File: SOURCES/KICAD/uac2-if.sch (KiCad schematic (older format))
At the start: 55 parts, among them IC24 XE216-512-TQ128, IC25 NCP4681DSQ25T1G, IC26 IS25LQ080B, IC301 NC7WZ07, X5 CONN_01X04, X6 USB_B, X7 CONN_02X10

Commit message: New PCB layout
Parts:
- removed C241: 10n0, rklib:C0805-X7R, symbol C
- removed C242, C243, C245, C301: 100n, rklib:C0805-X7R, symbol C
- removed C244: 1n00, rklib:C0805-X7R, symbol C
- removed C246, C247: 10u0, rklib:C0805-X7R, symbol C
- removed R249, R301, R302: 10K0, rklib:C0805-RES, symbol R
- removed R252: 33R0, Resistors_SMD:R_Array_Convex_4x0603, symbol R_PACK4
- removed R259: 100K, rklib:C0805-RES, symbol R
- removed X6: USB_B, Connect:USB_B, symbol USB_B
- removed X7: CONN_02X10, Pin_Headers:Pin_Header_Straight_2x10, symbol CONN_02X10
- added C201: CAP_10n0_50V_X7R_0805, rklib:C0805-X7R, symbol CAP_10n0_50V_X7R_0805
- added C202, C203, C204, C207: CAP_100n_50V_X7R_0805, rklib:C0805-X7R, symbol CAP_100n_50V_X7R_0805
- added C205, C206: CAP_10u0_25V_X5R_0805, rklib:C0805-X7R, symbol CAP_10u0_25V_X5R_0805
- added C208: CAP_1n00_50V_X7R_0805, rklib:C0805-X7R, symbol CAP_1n00_50V_X7R_0805
- added R201, R204, R205: RES_10K0_1%_0.125W_Thick_0805, rklib:C0805-RES, symbol RES_10K0_1%_0.25W_Thin_0805
- added R206: 51R0, Resistors_SMD:R_Array_Convex_4x0603, symbol R_Pack04
- added R213, R214: RES_2K00_1%_0.125W_Thick_0805, rklib:C0805-RES, symbol RES_4K70_1%_0.125W_Thick_0805
- added R215: RES_100K_1%_0.125W_Thick_0805, rklib:C0805-RES, symbol RES_100K_1%_0.125W_Thick_0805
- added X201: USB_B, Connect:USB_B, symbol USB_B
- added X203: HDR_02x10, Pin_Headers:Pin_Header_Straight_2x10, symbol Conn_02x10_Odd_Even
- IC204: renamed from IC26; value IS25LQ080B -> IS25LP080D
- R202: renamed from R250; value 33R0 -> 51R0
- R207: renamed from R253; value 33R0 -> 51R0
- R208: renamed from R254; value 33R0 -> 51R0
- R211: renamed from R257; value 33R0 -> 51R0
- R212: renamed from R258; value 33R0 -> 51R0
- X202: renamed from X5; symbol CONN_01X04 -> Conn_01x04
- renumbered C248 to C209, C249 to C210, C250 to C211, C251 to C212, C252 to C213, C253 to C214, C254 to C215, C255 to C216, C256 to C217, C257 to C218, C258 to C219, C259 to C220, C260 to C221, C261 to C222, C262 to C223, C263 to C224, C264 to C225, C265 to C226, C266 to C227, C267 to C228, C268 to C229, C269 to C230, C270 to C231, C271 to C232, C272 to C233, D65 to D201, IC301 to IC201, IC24 to IC202, IC25 to IC203, OSC1 to OSC201, R251 to R203, R255 to R209, R256 to R210
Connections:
- net labels removed: xSCL, xSDA
- wire segments 173 -> 181
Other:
- moved on the sheet: D201

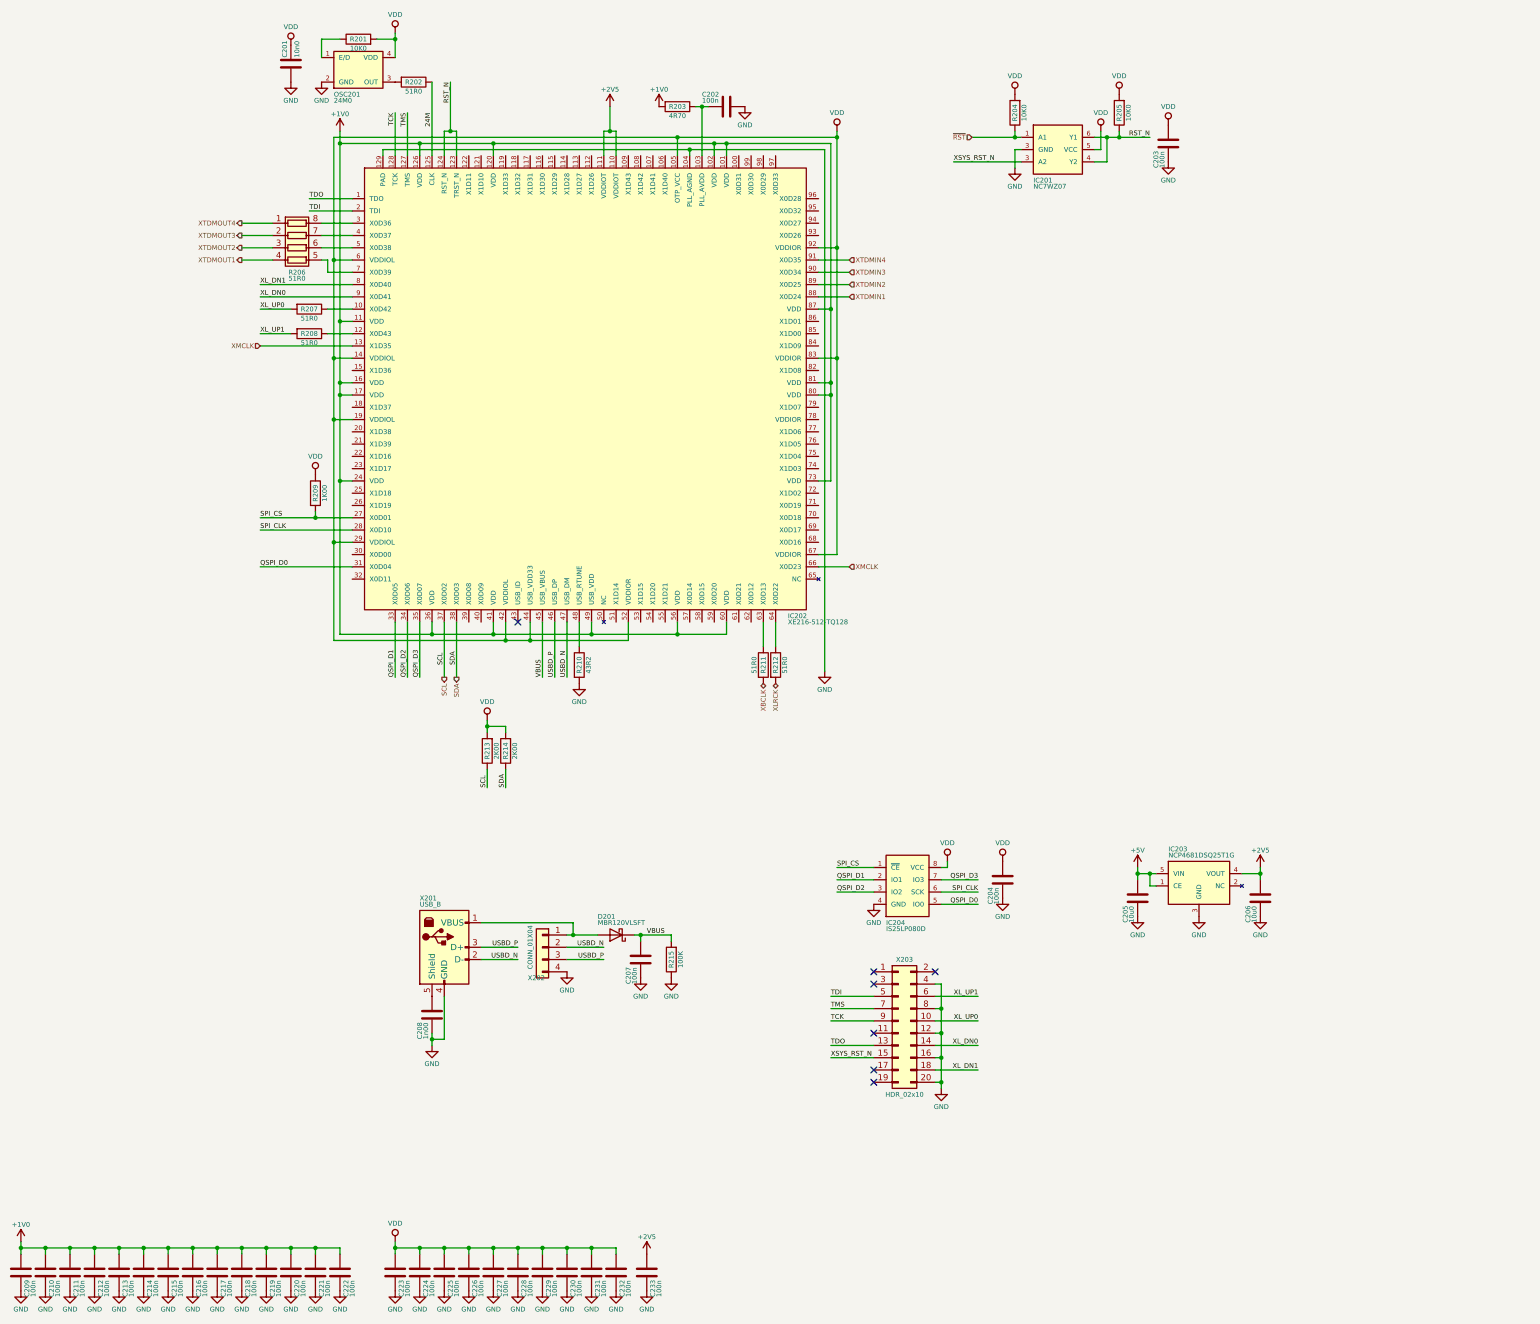
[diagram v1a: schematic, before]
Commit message: Bugfix on i2c multiplexer
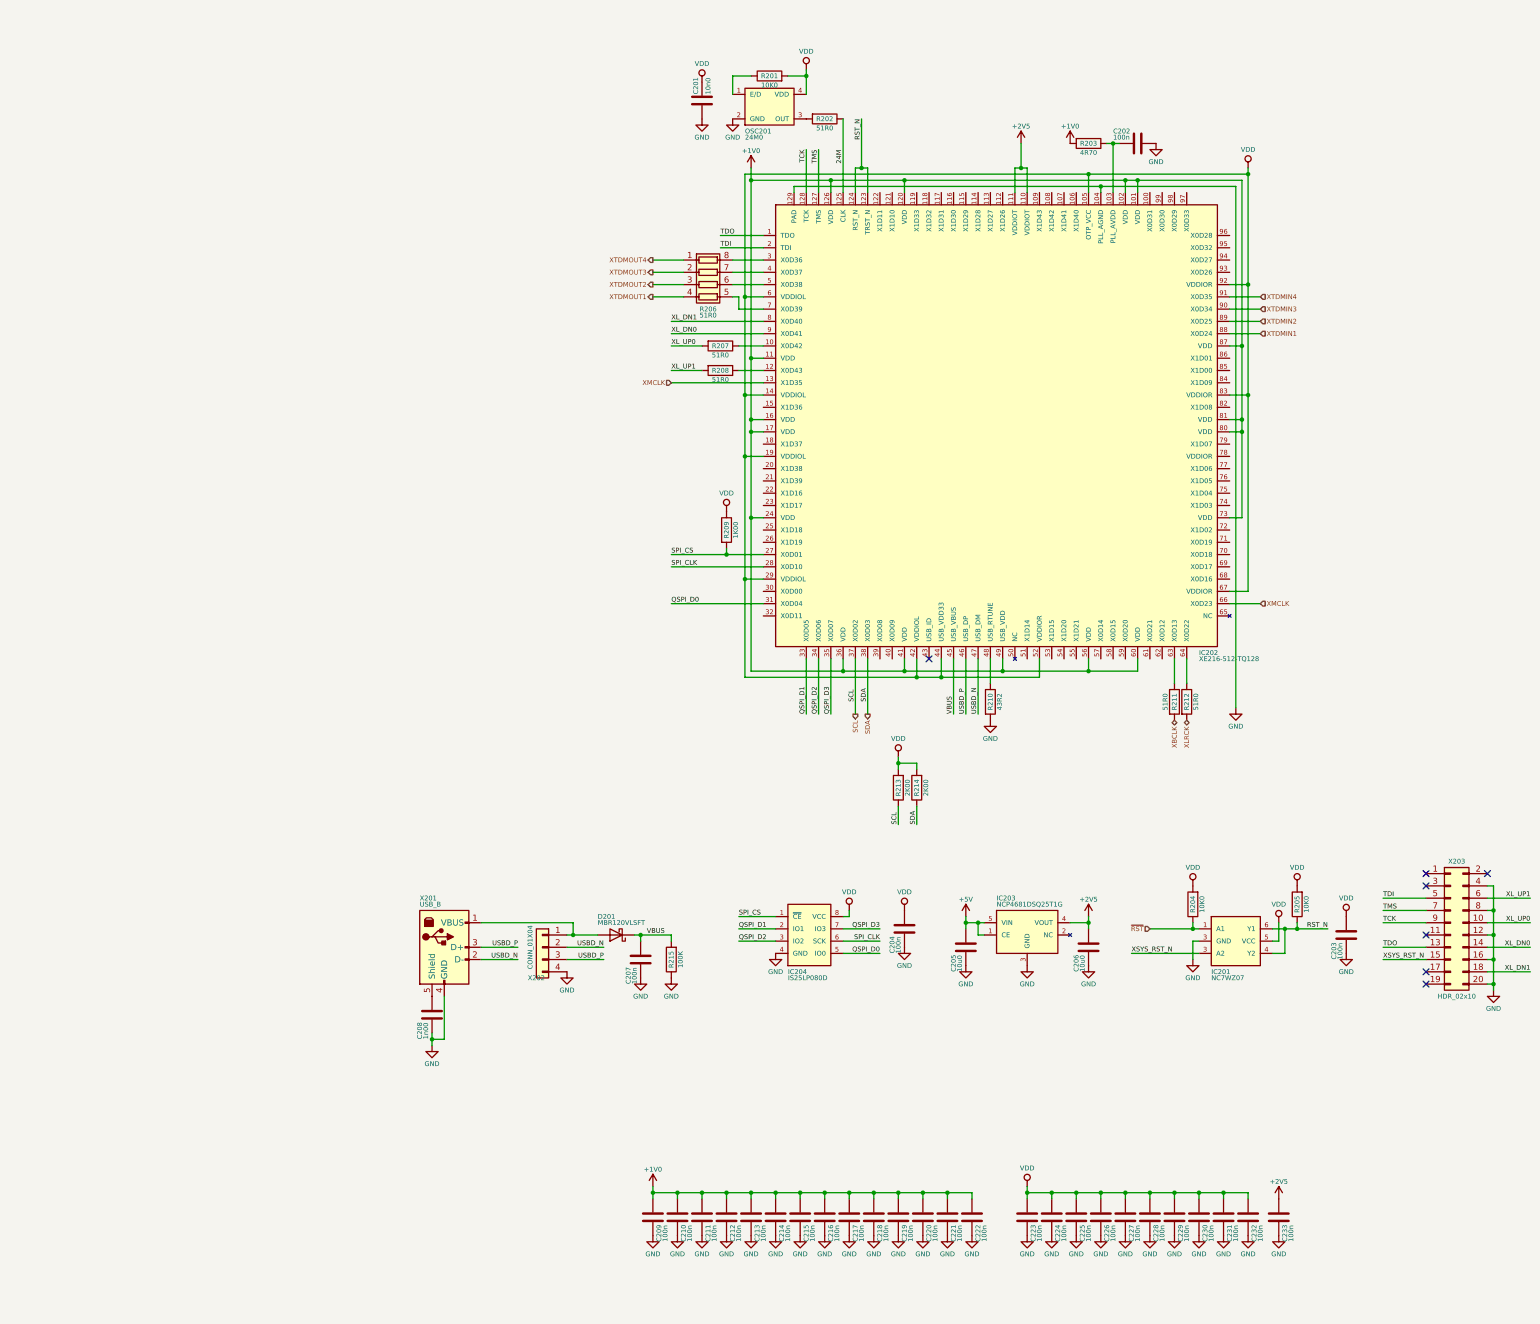
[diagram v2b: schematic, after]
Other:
- moved on the sheet: C201, C202, C203, C204, C205, C206, C209, C210, C211, C212, C213, C214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

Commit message: Changed USBi connector
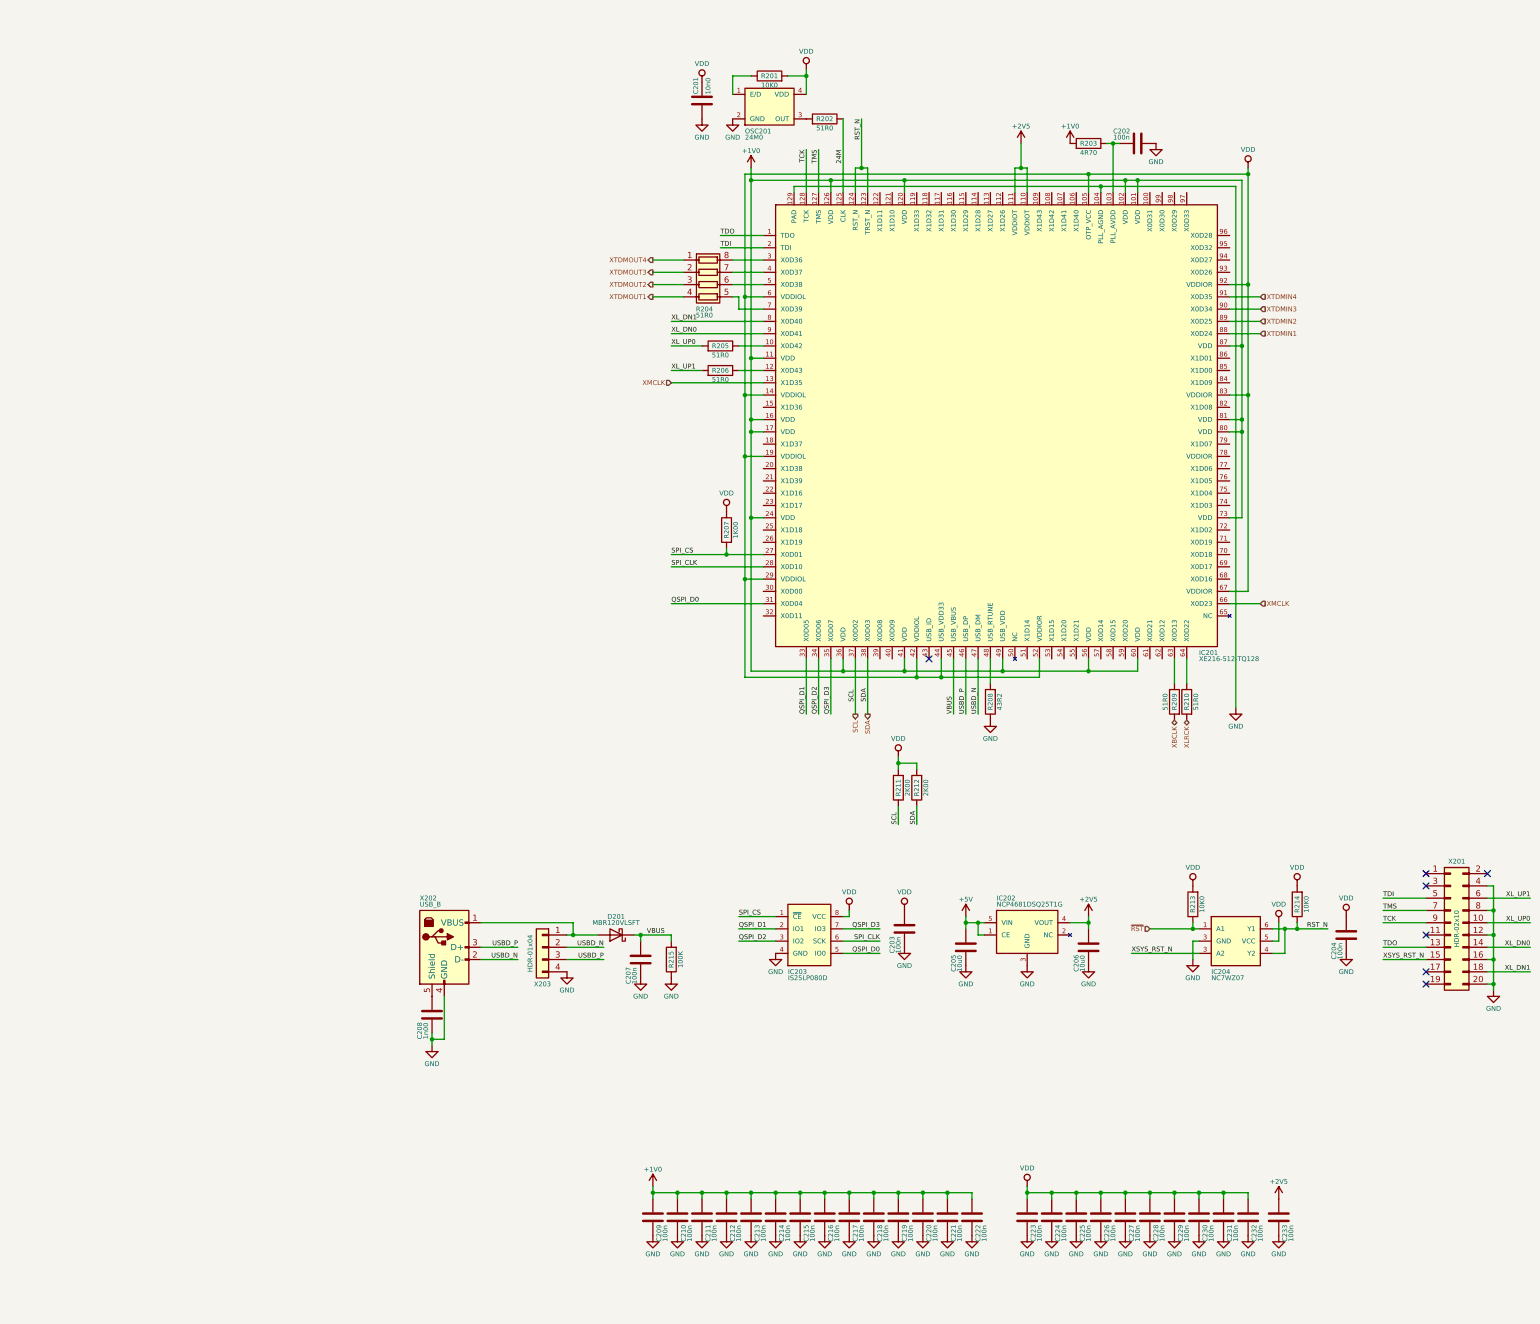
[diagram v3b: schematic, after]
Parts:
- removed C209, C210, C211, C212, C213, C214, C215, C216, C217, C218, C219, C220, C221, C222, C223, C224, C225, C226, C227, C228, C229, C230, C231, C232, C233: 100n, Capacitors_SMD:C_0402, symbol C
- removed D201: MBR120VLSFT, Diodes_SMD:SOD-123, symbol D_Schottky
- removed IC201: NC7WZ07, TO_SOT_Packages_SMD:SC-70-6, symbol NC7WZ07
- removed IC202: XE216-512-TQ128, rklib:TQFP-128_14x14mm_Pitch0.4mm_EP_Handsoldering, symbol XE216-512-TQ128
- removed IC203: NCP4681DSQ25T1G, TO_SOT_Packages_SMD:SC-70-5, symbol NCP4681DSQ25T1G
- removed IC204: IS25LP080D, Housings_SOIC:SOIC-8_3.9x4.9mm_Pitch1.27mm, symbol IS25LQ080B
- removed OSC201: 24M0, rklib:ASFL1, symbol 24MHz576
- removed R202, R207, R208, R211, R212: 51R0, rklib:C0805-RES, symbol R
- removed R203: 4R70, rklib:C0805-RES, symbol R
- removed R206: 51R0, Resistors_SMD:R_Array_Convex_4x0603, symbol R_Pack04
- removed R209: 1K00, rklib:C0805-RES, symbol R
- removed R210: 43R2, rklib:C0805-RES, symbol R
- removed X201: USB_B, Connect:USB_B, symbol USB_B
- removed X202: CONN_01X04, Pin_Headers:Pin_Header_Straight_1x04, symbol Conn_01x04
- removed X203: HDR_02x10, Pin_Headers:Pin_Header_Straight_2x10, symbol Conn_02x10_Odd_Even
- added C209, C210, C211, C212, C213, C214, C215, C216, C217, C218, C219, C220, C221, C222, C223, C224, C225, C226, C227, C228, C229, C230, C231, C232, C233: CAP_100n_10V_X7R_0402, Capacitors_SMD:C_0402, symbol CAP_100n_10V_X7R_0402
- added D201: DIO_MBR120VLSFT, rklib:SOD123, symbol DIO_MBR120VLSFT
- added IC201: IC_XE216-512-TQ128, rklib:TQFP-128_14x14mm_Pitch0.4mm_EP_Handsoldering, symbol IC_XE216-512-TQ128
- added IC202: IC_NCP4681DSQ25T1G, TO_SOT_Packages_SMD:SC-70-5, symbol IC_NCP4681DSQ25T1G
- added IC203: IC_IS25LP080D, rklib:SOIC8_3.9x4.9mm_Pitch1.27mm, symbol IC_IS25LP080D
- added IC204: IC_NC7WZ07, TO_SOT_Packages_SMD:SC-70-6, symbol IC_NC7WZ07
- added OSC201: OSC_24M0, rklib:ASFL1, symbol OSC_24M0
- added R202, R205, R206, R209, R210: RES_51R0_1%_0.125W_Thick_0805, rklib:C0805-RES, symbol RES_51R0_1%_0.125W_Thick_0805
- added R203: RES_4R70_1%_0.125W_Thick_0805, rklib:C0805-RES, symbol RES_4R70_1%_0.125W_Thick_0805
- added R204: RES_51R0_5%_4x0603, Resistors_SMD:R_Array_Convex_4x0603, symbol RES_51R0_5%_4x0603
- added R207: RES_1K00_1%_0.125W_Thick_0805, rklib:C0805-RES, symbol RES_1K00_1%_0.125W_Thick_0805
- added R208: RES_43R2_1%_0.125W_Thick_0805, rklib:C0805-RES, symbol RES_43R2_1%_0.125W_Thick_0805
- added X201: CON_HDR_02x10, rklib:HDR_02x10, symbol CON_HDR_02x10
- added X202: CON_USB_B, rklib:USB_B, symbol CON_USB_B
- added X203: CON_HDR_01x04, rklib:HDR_01x04, symbol CON_HDR_01x04
- R201: digikey ??? -> 311-10.0KCRCT-ND
- R211: renamed from R213; digikey ??? -> 311-2.00KCRCT-ND
- R212: renamed from R214; digikey ??? -> 311-2.00KCRCT-ND
- R213: renamed from R204; digikey ??? -> 311-10.0KCRCT-ND
- R214: renamed from R205; digikey ??? -> 311-10.0KCRCT-ND
- renumbered C204 to C203, C203 to C204
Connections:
- net +1V0: now also C209.1, C210.1, C211.1, C212.1, C213.1, C214.1, C215.1, C216.1, C217.1, C218.1, C219.1, C220.1, C221.1, C222.1, IC201.101 (VDD), IC201.102 (VDD), IC201.11 (VDD), IC201.120 (VDD), IC201.126 (VDD), IC201.16 (VDD), IC201.17 (VDD), IC201.24 (VDD), IC201.36 (VDD), IC201.41 (VDD), IC201.49 (USB_VDD), IC201.56 (VDD), IC201.60 (VDD), IC201.73 (VDD), IC201.80 (VDD), IC201.81 (VDD), IC201.87 (VDD), R203.2
- net +2V5: now also C233.1, IC201.110 (VDDIOT), IC201.111 (VDDIOT), IC202.4 (VOUT)
- net +5V: now also IC202.1 (CE), IC202.5 (VIN)
- net 24M: now also IC201.125 (CLK), R202.1
- net GND: now also C209.2, C210.2, C211.2, C212.2, C213.2, C214.2, C215.2, C216.2, C217.2, C218.2, C219.2, C220.2, C221.2, C222.2, C223.2, C224.2, C225.2, C226.2, C227.2, C228.2, C229.2, C230.2, C231.2, C232.2, C233.2, IC201.104 (PLL_AGND), IC201.129 (PAD), IC202.3 (GND), IC203.4 (GND), IC204.3 (GND), OSC201.2 (GND), R208.1, X201.12 (Pin_12), X201.16 (Pin_16), X201.20 (Pin_20), X201.4 (Pin_4), X201.8 (Pin_8), X202.4 (GND), X203.4 (Pin_4)
- net QSPI_D0: now also IC201.31 (X0D04), IC203.5 (IO0)
- net QSPI_D1: now also IC201.33 (X0D05), IC203.2 (IO1)
- net QSPI_D2: now also IC201.34 (X0D06), IC203.3 (IO2)
- net QSPI_D3: now also IC201.35 (X0D07), IC203.7 (IO3)
- net RST_N: now also IC201.123 (TRST_N), IC201.124 (RST_N), IC204.4 (Y2), IC204.6 (Y1)
- net SCL: now also IC201.37 (X0D02)
- net SDA: now also IC201.38 (X0D03)
- net SPI_CLK: now also IC201.28 (X0D10), IC203.6 (SCK)
- net SPI_CS: now also IC201.27 (X0D01), IC203.1 (~CE), R207.2
- net TCK: now also IC201.128 (TCK), X201.9 (Pin_9)
- net TDI: now also IC201.2 (TDI), X201.5 (Pin_5)
- net TDO: now also IC201.1 (TDO), X201.13 (Pin_13)
- net TMS: now also IC201.127 (TMS), X201.7 (Pin_7)
- net USBD_N: now also IC201.47 (USB_DM), X202.2 (D-), X203.2 (Pin_2)
- net USBD_P: now also IC201.46 (USB_DP), X202.3 (D+), X203.3 (Pin_3)
- net VBUS: now also D201.1 (K), IC201.45 (USB_VBUS)
- net VDD: now also C223.1, C224.1, C225.1, C226.1, C227.1, C228.1, C229.1, C230.1, C231.1, C232.1, IC201.105 (OTP_VCC), IC201.14 (VDDIOL), IC201.19 (VDDIOL), IC201.29 (VDDIOL), IC201.42 (VDDIOL), IC201.44 (USB_VDD33), IC201.52 (VDDIOR), IC201.6 (VDDIOL), IC201.67 (VDDIOR), IC201.83 (VDDIOR), IC201.92 (VDDIOR), IC203.8 (VCC), IC204.5 (VCC), OSC201.4 (VDD), R207.1
- net XBCLK: now also R209.2
- net XLRCK: now also R210.2
- net XL_DN0: now also IC201.9 (X0D41), X201.14 (Pin_14)
- net XL_DN1: now also IC201.8 (X0D40), X201.18 (Pin_18)
- net XL_UP0: now also R205.2, X201.10 (Pin_10)
- net XL_UP1: now also R206.2, X201.6 (Pin_6)
- net XMCLK: now also IC201.13 (X1D35), IC201.66 (X0D23)
- net XSYS_RST_N: now also IC204.3 (GND), X201.15 (Pin_15)
- net XTDMIN1: now also IC201.88 (X0D24)
- net XTDMIN2: now also IC201.89 (X0D25)
- net XTDMIN3: now also IC201.90 (X0D34)
- net XTDMIN4: now also IC201.91 (X0D35)
- net XTDMOUT1: now also R204.4 (R4.1)
- net XTDMOUT2: now also R204.3 (R3.1)
- net XTDMOUT3: now also R204.2 (R2.1)
- net XTDMOUT4: now also R204.1 (R1.1)
- net ~RST: now also IC204.1 (A1)
- net at C202.1: now also IC201.103 (PLL_AVDD), R203.1
- net at R201.1: now also OSC201.1 (E/D)
- net at C208.2: now also X202.5 (Shield)
- new net: D201.2 (A), X202.1 (VBUS), X203.1 (Pin_1)
- new net: OSC201.3 (OUT), R202.2
- new net: IC201.10 (X0D42), R205.1
- new net: IC201.12 (X0D43), R206.1
- new net: IC201.3 (X0D36), R204.8 (R1.2)
- new net: IC201.4 (X0D37), R204.7 (R2.2)
- new net: IC201.48 (USB_RTUNE), R208.2
- new net: IC201.5 (X0D38), R204.6 (R3.2)
- new net: IC201.63 (X0D13), R209.1
- new net: IC201.64 (X0D22), R210.1
- new net: IC201.7 (X0D39), R204.5 (R4.2)

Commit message: Upgraded to KiCAD 5
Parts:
- C201: symbol CAP_10n0_50V_X7R_0805 -> rk:CAP_10n0_50V_X7R_0805
- C202, C203, C204, C207: symbol CAP_100n_50V_X7R_0805 -> rk:CAP_100n_50V_X7R_0805
- C205, C206: symbol CAP_10u0_25V_X5R_0805 -> rk:CAP_10u0_25V_X5R_0805
- C208: symbol CAP_1n00_50V_X7R_0805 -> rk:CAP_1n00_50V_X7R_0805
- C209, C210, C211, C212, C213, C214, C215, C216, C217, C218, C219, C220, C221, C222, C223, C224, C225, C226, C227, C228, C229, C230, C231, C232, C233: symbol CAP_100n_10V_X7R_0402 -> rk:CAP_100n_10V_X7R_0402
- D201: symbol DIO_MBR120VLSFT -> rk:DIO_MBR120VLSFT
- IC201: symbol IC_XE216-512-TQ128 -> rk:IC_XE216-512-TQ128
- IC202: symbol IC_NCP4681DSQ25T1G -> rk:IC_NCP4681DSQ25T1G
- IC203: symbol IC_IS25LP080D -> rk:IC_IS25LP080D
- IC204: symbol IC_NC7WZ07 -> rk:IC_NC7WZ07
- OSC201: symbol OSC_24M0 -> rk:OSC_24M0
- R201, R213, R214: symbol RES_10K0_1%_0.25W_Thin_0805 -> rk:RES_10K0_1%_0.25W_Thin_0805
- R202, R205, R206, R209, R210: symbol RES_51R0_1%_0.125W_Thick_0805 -> rk:RES_51R0_1%_0.125W_Thick_0805
- R203: symbol RES_4R70_1%_0.125W_Thick_0805 -> rk:RES_4R70_1%_0.125W_Thick_0805
- R204: symbol RES_51R0_5%_4x0603 -> rk:RES_51R0_5%_4x0603
- R207: symbol RES_1K00_1%_0.125W_Thick_0805 -> rk:RES_1K00_1%_0.125W_Thick_0805
- R208: symbol RES_43R2_1%_0.125W_Thick_0805 -> rk:RES_43R2_1%_0.125W_Thick_0805
- R211, R212: symbol RES_4K70_1%_0.125W_Thick_0805 -> rk:RES_4K70_1%_0.125W_Thick_0805
- R215: symbol RES_100K_1%_0.125W_Thick_0805 -> rk:RES_100K_1%_0.125W_Thick_0805
- X201: symbol CON_HDR_02x10 -> rk:CON_HDR_02x10
- X202: symbol CON_USB_B -> rk:CON_USB_B
- X203: symbol CON_HDR_01x04 -> rk:CON_HDR_01x04
